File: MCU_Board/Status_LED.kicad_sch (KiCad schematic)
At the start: 12 parts, among them Q1 MMBT3904, Q2 MMBT3904, Q3 MMBT3904

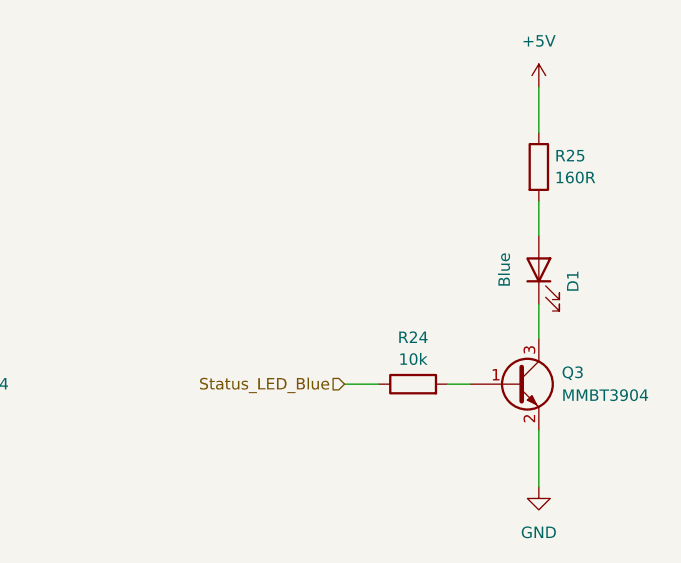
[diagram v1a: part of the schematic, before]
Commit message: Added JTAG connector to MCU board
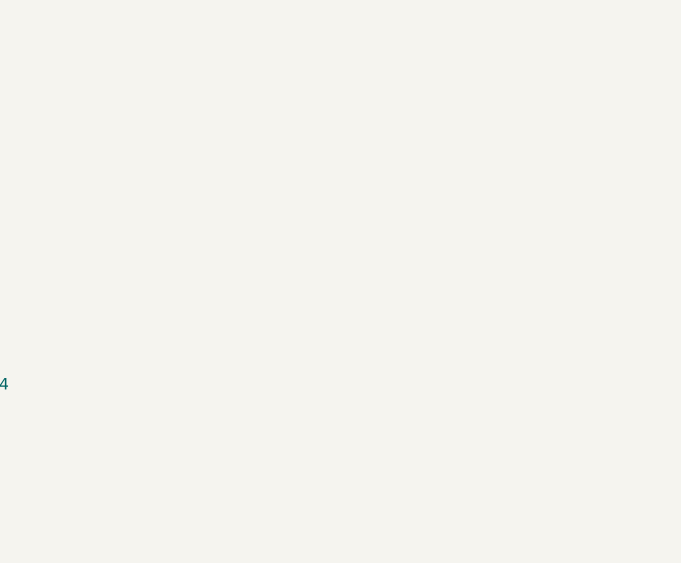
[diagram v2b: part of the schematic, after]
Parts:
- removed D1: Blue, LED_THT:LED_D4.0mm, symbol Device:LED
- removed Q3: MMBT3904, Package_TO_SOT_SMD:SOT-23, symbol Transistor_BJT:MMBT3904
- removed R24: 10k, Resistor_SMD:R_0603_1608Metric_Pad0.98x0.95mm_HandSolder, symbol Device:R
- removed R25: 160R, Resistor_SMD:R_0603_1608Metric_Pad0.98x0.95mm_HandSolder, symbol Device:R
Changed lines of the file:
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@@
 (kicad_sch (version 20230121) (generator eeschema)
   (paper "A4")
-  (wire (pts (xy 194.31 88.9) (xy 196.85 88.9))
-    (stroke (width 0) (type default))
-  )
   (wire (pts (xy 133.35 54.61) (xy 133.35 59.69))
     (stroke (width 0) (type default))
@@
     (stroke (width 0) (type default))
   )
-  (wire (pts (xy 204.47 55.88) (xy 204.47 60.96))
-    (stroke (width 0) (type default))
-  )
-  (wire (pts (xy 204.47 80.01) (xy 204.47 83.82))
-    (stroke (width 0) (type default))
-  )
   (wire (pts (xy 58.42 78.74) (xy 58.42 82.55))
     (stroke (width 0) (type default))
@@
     (stroke (width 0) (type default))
   )
-  (wire (pts (xy 182.88 88.9) (xy 186.69 88.9))
-    (stroke (width 0) (type default))
-  )
   (wire (pts (xy 58.42 54.61) (xy 58.42 59.69))
     (stroke (width 0) (type default))
@@
     (stroke (width 0) (type default))
   )
-  (wire (pts (xy 204.47 100.33) (xy 204.47 93.98))
-    (stroke (width 0) (type default))
-  )
-  (wire (pts (xy 204.47 68.58) (xy 204.47 72.39))
-    (stroke (width 0) (type default))
-  )
   (wire (pts (xy 58.42 67.31) (xy 58.42 71.12))
     (stroke (width 0) (type default))
@@
   (wire (pts (xy 123.19 87.63) (xy 125.73 87.63))
     (stroke (width 0) (type default))
-  )
-  (hierarchical_label "Status_LED_Blue" (shape input) (at 182.88 88.9 180) (fields_autoplaced)
-    (effects (font (size 1.27 1.27)) (justify right))
   )
   (hierarchical_label "Status_LED_Green" (shape input) (at 36.83 87.63 180) (fields_autoplaced)
@@
   (hierarchical_label "Status_LED_Red" (shape input) (at 106.68 87.63 180) (fields_autoplaced)
     (effects (font (size 1.27 1.27)) (justify right))
-  )
-  (symbol (lib_id "Device:R") (at 204.47 64.77 0) (unit 1)
-    (in_bom yes) (on_board yes) (dnp no) (fields_autoplaced)
-    (property "Reference" "R25" (at 206.248 63.5579 0)
-      (effects (font (size 1.27 1.27)) (justify left))
-    )
-    (property "Value" "160R" (at 206.248 65.9821 0)
-      (effects (font (size 1.27 1.27)) (justify left))
-    )
-    (property "Footprint" "Resistor_SMD:R_0603_1608Metric_Pad0.98x0.95mm_HandSolder" (at 202.692 64.77 90)
-      (effects (font (size 1.27 1.27)) hide)
-    )
-    (property "Datasheet" "~" (at 204.47 64.77 0)
-      (effects (font (size 1.27 1.27)) hide)
-    )
-    (pin "1")
-    (pin "2")
-    (instances
-      (project "MCU_Board"
-        (path "/29349b68-071c-451b-9b1e-10b5ef7e12a6/8e6d62a1-615e-4e74-ad33-9284c4715f87/15f14a7a-b8b3-478a-b13a-51796c28d4d6"
-          (reference "R25") (unit 1)
-        )
-      )
-    )
   )
   (symbol (lib_id "Device:LED") (at 133.35 74.93 90) (unit 1)
@@
     )
   )
-  (symbol (lib_id "power:+5V") (at 204.47 55.88 0) (unit 1)
-    (in_bom yes) (on_board yes) (dnp no) (fields_autoplaced)
-    (property "Reference" "#PWR053" (at 204.47 59.69 0)
-      (effects (font (size 1.27 1.27)) hide)
-    )
-    (property "Value" "+5V" (at 204.47 50.8 0)
-      (effects (font (size 1.27 1.27)))
-    )
-    (property "Footprint" "" (at 204.47 55.88 0)
-      (effects (font (size 1.27 1.27)) hide)
-    )
-    (property "Datasheet" "" (at 204.47 55.88 0)
-      (effects (font (size 1.27 1.27)) hide)
-    )
-    (pin "1")
-    (instances
-      (project "MCU_Board"
-        (path "/29349b68-071c-451b-9b1e-10b5ef7e12a6/8e6d62a1-615e-4e74-ad33-9284c4715f87/15f14a7a-b8b3-478a-b13a-51796c28d4d6"
-          (reference "#PWR053") (unit 1)
-        )
-      )
-    )
-  )
   (symbol (lib_id "Device:LED") (at 58.42 74.93 90) (unit 1)
     (in_bom yes) (on_board yes) (dnp no)
@@
     )
   )
-  (symbol (lib_id "power:GND") (at 204.47 100.33 0) (unit 1)
-    (in_bom yes) (on_board yes) (dnp no) (fields_autoplaced)
-    (property "Reference" "#PWR055" (at 204.47 106.68 0)
-      (effects (font (size 1.27 1.27)) hide)
-    )
-    (property "Value" "GND" (at 204.47 105.41 0)
-      (effects (font (size 1.27 1.27)))
-    )
-    (property "Footprint" "" (at 204.47 100.33 0)
-      (effects (font (size 1.27 1.27)) hide)
-    )
-    (property "Datasheet" "" (at 204.47 100.33 0)
-      (effects (font (size 1.27 1.27)) hide)
-    )
-    (pin "1")
-    (instances
-      (project "MCU_Board"
-        (path "/29349b68-071c-451b-9b1e-10b5ef7e12a6/8e6d62a1-615e-4e74-ad33-9284c4715f87/15f14a7a-b8b3-478a-b13a-51796c28d4d6"
-          (reference "#PWR055") (unit 1)
-        )
-      )
-    )
-  )
   (symbol (lib_id "Device:R") (at 58.42 63.5 0) (unit 1)
     (in_bom yes) (on_board yes) (dnp no) (fields_autoplaced)
@@
         )
       )
-    )
-  )
-  (symbol (lib_id "Device:LED") (at 204.47 76.2 90) (unit 1)
-    (in_bom yes) (on_board yes) (dnp no)
-    (property "Reference" "D1" (at 208.28 77.47 0)
-      (effects (font (size 1.27 1.27)))
-    )
-    (property "Value" "Blue" (at 200.66 76.2 0)
-      (effects (font (size 1.27 1.27)))
-    )
-    (property "Footprint" "LED_THT:LED_D4.0mm" (at 204.47 76.2 0)
-      (effects (font (size 1.27 1.27)) hide)
-    )
-    (property "Datasheet" "~" (at 204.47 76.2 0)
-      (effects (font (size 1.27 1.27)) hide)
-    )
-    (pin "1")
-    (pin "2")
-    (instances
-      (project "MCU_Board"
-        (path "/29349b68-071c-451b-9b1e-10b5ef7e12a6/8e6d62a1-615e-4e74-ad33-9284c4715f87"
-          (reference "D1") (unit 1)
-        )
-        (path "/29349b68-071c-451b-9b1e-10b5ef7e12a6/8e6d62a1-615e-4e74-ad33-9284c4715f87/15f14a7a-b8b3-478a-b13a-51796c28d4d6"
-          (reference "D3") (unit 1)
-        )
-      )
-    )
-  )
-  (symbol (lib_id "Transistor_BJT:MMBT3904") (at 201.93 88.9 0) (unit 1)
-    (in_bom yes) (on_board yes) (dnp no) (fields_autoplaced)
-    (property "Reference" "Q3" (at 207.01 87.63 0)
-      (effects (font (size 1.27 1.27)) (justify left))
-    )
-    (property "Value" "MMBT3904" (at 207.01 90.17 0)
-      (effects (font (size 1.27 1.27)) (justify left))
-    )
-    (property "Footprint" "Package_TO_SOT_SMD:SOT-23" (at 207.01 90.805 0)
-      (effects (font (size 1.27 1.27) italic) (justify left) hide)
-    )
-    (property "Datasheet" "https://www.onsemi.com/pub/Collateral/2N3903-D.PDF" (at 201.93 88.9 0)
-      (effects (font (size 1.27 1.27)) (justify left) hide)
-    )
-    (pin "1")
-    (pin "2")
-    (pin "3")
-    (instances
-      (project "MCU_Board"
-        (path "/29349b68-071c-451b-9b1e-10b5ef7e12a6/8e6d62a1-615e-4e74-ad33-9284c4715f87/15f14a7a-b8b3-478a-b13a-51796c28d4d6"
-          (reference "Q3") (unit 1)
-        )
-      )
-    )
-  )
-  (symbol (lib_id "Device:R") (at 190.5 88.9 90) (unit 1)
-    (in_bom yes) (on_board yes) (dnp no) (fields_autoplaced)
-    (property "Reference" "R24" (at 190.5 83.7397 90)
-      (effects (font (size 1.27 1.27)))
-    )
-    (property "Value" "10k" (at 190.5 86.1639 90)
-      (effects (font (size 1.27 1.27)))
-    )
-    (property "Footprint" "Resistor_SMD:R_0603_1608Metric_Pad0.98x0.95mm_HandSolder" (at 190.5 90.678 90)
-      (effects (font (size 1.27 1.27)) hide)
-    )
-    (property "Datasheet" "~" (at 190.5 88.9 0)
-      (effects (font (size 1.27 1.27)) hide)
-    )
-    (pin "1")
-    (pin "2")
-    (instances
-      (project "MCU_Board"
-        (path "/29349b68-071c-451b-9b1e-10b5ef7e12a6/8e6d62a1-615e-4e74-ad33-9284c4715f87/15f14a7a-b8b3-478a-b13a-51796c28d4d6"
-          (reference "R24") (unit 1)
-        )
-      )

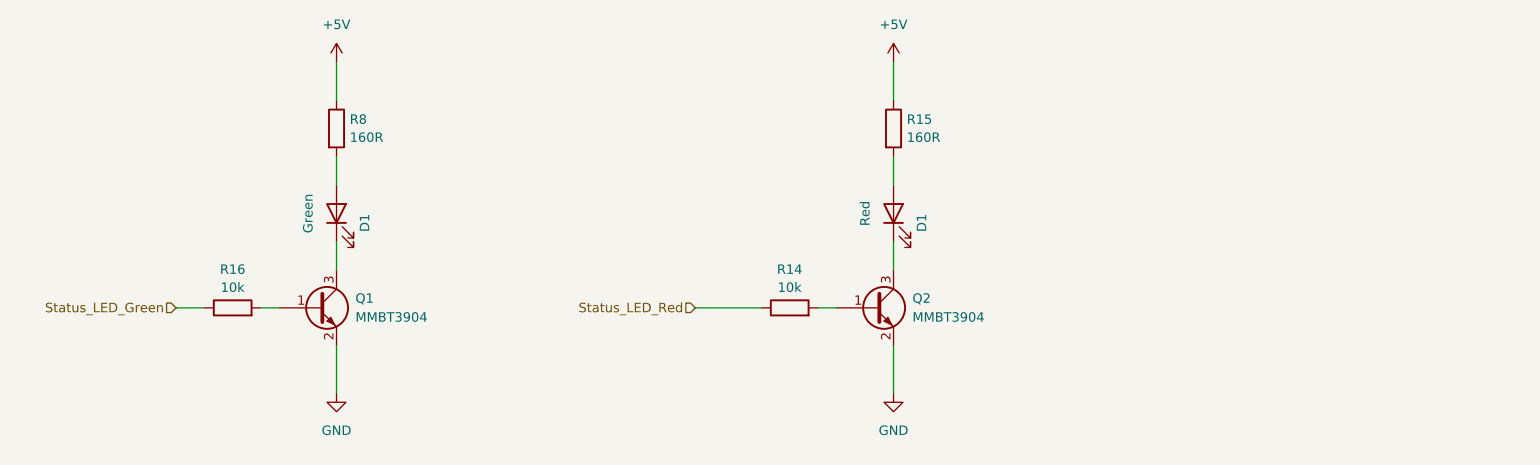
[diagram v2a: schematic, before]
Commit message: Finished MCU board
Finished MCU board and started finishing up the VCO board
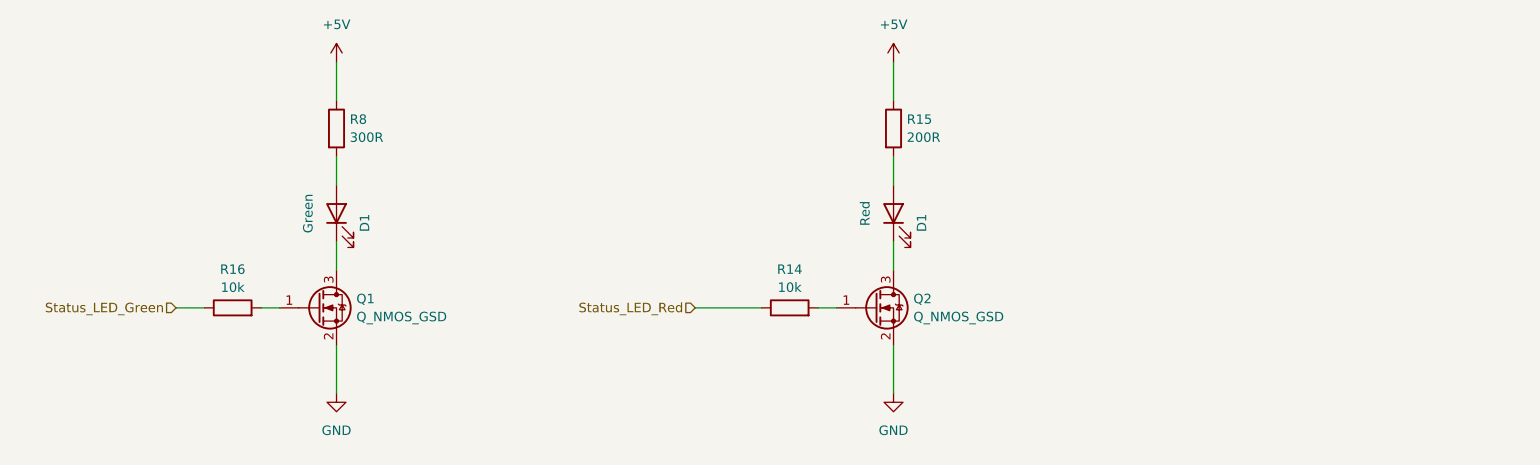
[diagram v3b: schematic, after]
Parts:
- removed Q1, Q2: MMBT3904, Package_TO_SOT_SMD:SOT-23, symbol Transistor_BJT:MMBT3904
- added Q1, Q2: Q_NMOS_GSD, Package_TO_SOT_SMD:SOT-23, symbol Device:Q_NMOS_GSD
- R14, R16: footprint Resistor_SMD:R_0603_1608Metric_Pad0.98x0.95mm_HandSolder -> Resistor_SMD:R_0402_1005Metric_Pad0.72x0.64mm_HandSolder
- R15: value 160R -> 200R
- R8: value 160R -> 300R
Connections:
- net GND: now also Q1.2 (S), Q2.2 (S)
- net at D1.1 (K): now also Q2.3 (D)
- net at D1.1 (K): now also Q1.3 (D)
- net at R16.2: now also Q1.1 (G)
- net at R14.2: now also Q2.1 (G)
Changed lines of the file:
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@@
       (effects (font (size 1.27 1.27)) (justify left))
     )
-    (property "Value" "160R" (at 135.128 64.7121 0)
+    (property "Value" "200R" (at 135.128 64.7121 0)
       (effects (font (size 1.27 1.27)) (justify left))
     )
@@
     )
   )
+  (symbol (lib_id "Device:Q_NMOS_GSD") (at 55.88 87.63 0) (unit 1)
+    (in_bom yes) (on_board yes) (dnp no) (fields_autoplaced)
+    (property "Reference" "Q1" (at 61.087 86.4179 0)
+      (effects (font (size 1.27 1.27)) (justify left))
+    )
+    (property "Value" "Q_NMOS_GSD" (at 61.087 88.8421 0)
+      (effects (font (size 1.27 1.27)) (justify left))
+    )
+    (property "Footprint" "Package_TO_SOT_SMD:SOT-23" (at 60.96 85.09 0)
+      (effects (font (size 1.27 1.27)) hide)
+    )
+    (property "Datasheet" "~" (at 55.88 87.63 0)
+      (effects (font (size 1.27 1.27)) hide)
+    )
+    (pin "1")
+    (pin "2")
+    (pin "3")
+    (instances
+      (project "MCU_Board"
+        (path "/29349b68-071c-451b-9b1e-10b5ef7e12a6/8e6d62a1-615e-4e74-ad33-9284c4715f87/15f14a7a-b8b3-478a-b13a-51796c28d4d6"
+          (reference "Q1") (unit 1)
+        )
+      )
+    )
+  )
   (symbol (lib_id "Device:R") (at 58.42 63.5 0) (unit 1)
     (in_bom yes) (on_board yes) (dnp no) (fields_autoplaced)
@@
       (effects (font (size 1.27 1.27)) (justify left))
     )
-    (property "Value" "160R" (at 60.198 64.7121 0)
+    (property "Value" "300R" (at 60.198 64.7121 0)
       (effects (font (size 1.27 1.27)) (justify left))
     )
@@
       (effects (font (size 1.27 1.27)))
     )
-    (property "Footprint" "Resistor_SMD:R_0603_1608Metric_Pad0.98x0.95mm_HandSolder" (at 44.45 89.408 90)
+    (property "Footprint" "Resistor_SMD:R_0402_1005Metric_Pad0.72x0.64mm_HandSolder" (at 44.45 89.408 90)
       (effects (font (size 1.27 1.27)) hide)
     )
@@
       (effects (font (size 1.27 1.27)))
     )
-    (property "Footprint" "Resistor_SMD:R_0603_1608Metric_Pad0.98x0.95mm_HandSolder" (at 119.38 89.408 90)
+    (property "Footprint" "Resistor_SMD:R_0402_1005Metric_Pad0.72x0.64mm_HandSolder" (at 119.38 89.408 90)
       (effects (font (size 1.27 1.27)) hide)
     )
@@
     )
   )
-  (symbol (lib_id "Transistor_BJT:MMBT3904") (at 130.81 87.63 0) (unit 1)
+  (symbol (lib_id "Device:Q_NMOS_GSD") (at 130.81 87.63 0) (unit 1)
     (in_bom yes) (on_board yes) (dnp no) (fields_autoplaced)
-    (property "Reference" "Q2" (at 135.89 86.36 0)
+    (property "Reference" "Q2" (at 136.017 86.4179 0)
       (effects (font (size 1.27 1.27)) (justify left))
     )
-    (property "Value" "MMBT3904" (at 135.89 88.9 0)
+    (property "Value" "Q_NMOS_GSD" (at 136.017 88.8421 0)
       (effects (font (size 1.27 1.27)) (justify left))
     )
-    (property "Footprint" "Package_TO_SOT_SMD:SOT-23" (at 135.89 89.535 0)
-      (effects (font (size 1.27 1.27) italic) (justify left) hide)
+    (property "Footprint" "Package_TO_SOT_SMD:SOT-23" (at 135.89 85.09 0)
+      (effects (font (size 1.27 1.27)) hide)
     )
-    (property "Datasheet" "https://www.onsemi.com/pub/Collateral/2N3903-D.PDF" (at 130.81 87.63 0)
-      (effects (font (size 1.27 1.27)) (justify left) hide)
+    (property "Datasheet" "~" (at 130.81 87.63 0)
+      (effects (font (size 1.27 1.27)) hide)
     )
     (pin "1")
@@
         )
       )
-    )
-  )
-  (symbol (lib_id "Transistor_BJT:MMBT3904") (at 55.88 87.63 0) (unit 1)
-    (in_bom yes) (on_board yes) (dnp no) (fields_autoplaced)
-    (property "Reference" "Q1" (at 60.96 86.36 0)
-      (effects (font (size 1.27 1.27)) (justify left))
-    )
-    (property "Value" "MMBT3904" (at 60.96 88.9 0)
-      (effects (font (size 1.27 1.27)) (justify left))
-    )
-    (property "Footprint" "Package_TO_SOT_SMD:SOT-23" (at 60.96 89.535 0)
-      (effects (font (size 1.27 1.27) italic) (justify left) hide)
-    )
-    (property "Datasheet" "https://www.onsemi.com/pub/Collateral/2N3903-D.PDF" (at 55.88 87.63 0)
-      (effects (font (size 1.27 1.27)) (justify left) hide)
-    )
-    (pin "1")
-    (pin "2")
-    (pin "3")
-    (instances
-      (project "MCU_Board"
-        (path "/29349b68-071c-451b-9b1e-10b5ef7e12a6/8e6d62a1-615e-4e74-ad33-9284c4715f87/15f14a7a-b8b3-478a-b13a-51796c28d4d6"
-          (reference "Q1") (unit 1)
-        )
-      )
